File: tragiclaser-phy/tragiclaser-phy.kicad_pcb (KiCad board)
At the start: 4 copper layers, 105 x 28.5 mm, 79 parts, among them J1 XILINX_JTAG, J2 BEL_FUSE_0826-1G1T-23-F, K1 CONN_3_PWROUT, P1 CONN_01X12, U1 XC6SLX25-2FTG256C, U2 ADP322ACPZ-145-R7, U3 DNP, U4 100 MHz

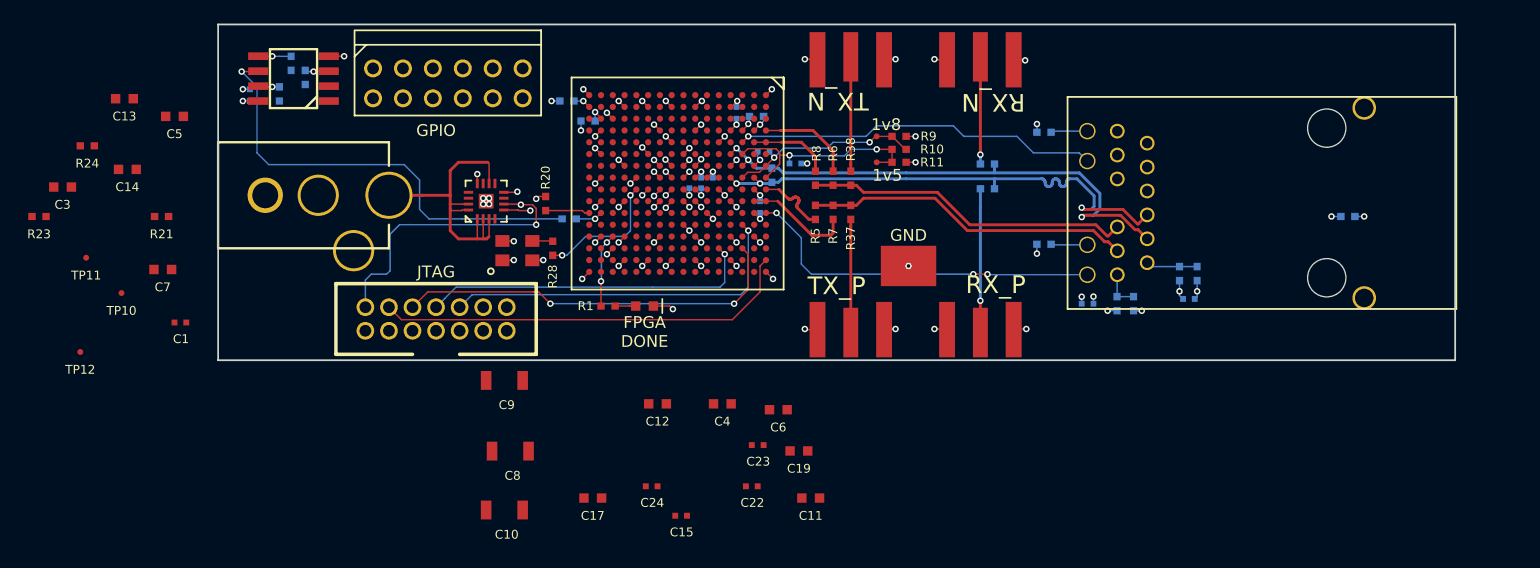
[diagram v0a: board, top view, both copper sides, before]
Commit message: Finished initial layout, ready for design review
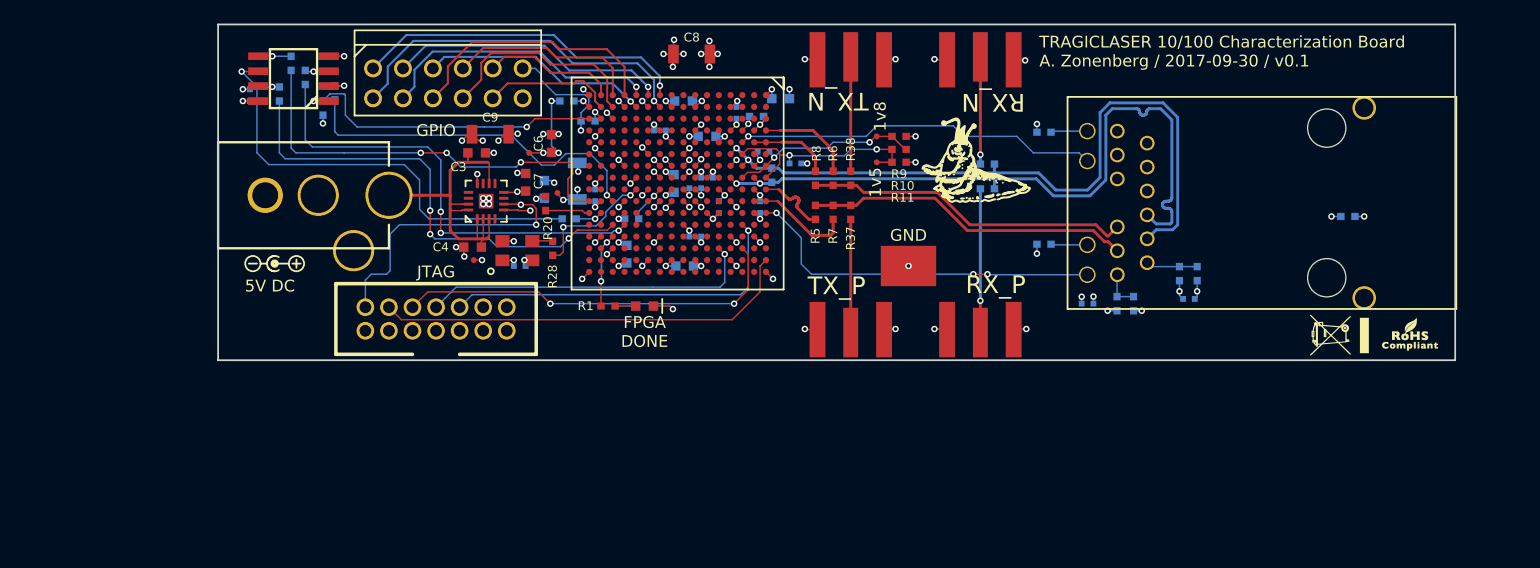
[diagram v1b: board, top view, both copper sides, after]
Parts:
- added G***: LOGO, azonenberg_pcb:LONGTHING-1200DPI, F.Cu at (142.9, 45.4)
- added G***: LOGO, w_logo:Logo_silk_WEEE_3.4x5mm, F.Cu at (173.2, 59.9)
- added G***: LOGO, w_logo:Logo_silk_ROHS_5x2.8mm, F.Cu at (179.2, 59.8)
- added G***: LOGO, w_logo:Logo_silk_polarity_center_5x1.4mm, F.Cu at (82.8, 53.8)
- C1, C10, C11, C12, C13, C14, C15, C17, C19, C22, C23, C24, C5, R21, R23, R24: moved to B.Cu
- moved C14 55.8 mm to (125.8, 39.8), turned to 180 degrees
- moved C13 47.2 mm to (116.7, 47.0), turned to 90 degrees
- moved TP12 42.7 mm to (106.8, 47.8)
- moved R21 39.9 mm to (113.1, 50.0), turned to 180 degrees
- moved TP11 38.6 mm to (104.4, 44.4)
- moved C8 37.1 mm to (118.2, 36.0)
- moved C11 35.4 mm to (117.5, 40.0)
- moved C3 35.3 mm to (100.0, 44.4)
- moved C5 32.0 mm to (105.7, 47.5), turned to 90 degrees
- moved C7 31.7 mm to (104.1, 46.9), turned to 90 degrees
- moved TP10 30.0 mm to (99.7, 53.5)
- moved C6 29.7 mm to (106.3, 43.6), turned to 90 degrees
- moved C1 29.2 mm to (103.6, 54.0)
- moved C10 28.6 mm to (108.5, 46.8), turned to 90 degrees
- moved C22 28.1 mm to (110.0, 48.0), turned to 270 degrees
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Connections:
- U1 pad A12: /PHY/GPIO1 -> Net-(U1-PadA12)
- U1 pad A13: /PHY/GPIO3 -> Net-(U1-PadA13)
- U1 pad A14: /PHY/GPIO5 -> Net-(U1-PadA14)
- U1 pad A2: (no net) -> Net-(U1-PadA2)
- U1 pad A3: (no net) -> Net-(U1-PadA3)
- U1 pad A6: /PHY/GPIO8 -> Net-(U1-PadA6)
- U1 pad B1: (no net) -> Net-(U1-PadB1)
- U1 pad B12: /PHY/GPIO0 -> Net-(U1-PadB12)
- U1 pad B14: /PHY/GPIO4 -> Net-(U1-PadB14)
- U1 pad B2: (no net) -> Net-(U1-PadB2)
- U1 pad B3: (no net) -> Net-(U1-PadB3)
- U1 pad B6: /PHY/GPIO7 -> Net-(U1-PadB6)
- U1 pad C1: (no net) -> Net-(U1-PadC1)
- U1 pad C11: /PHY/GPIO9 -> Net-(U1-PadC11)
- U1 pad C13: /PHY/GPIO2 -> Net-(U1-PadC13)
- U1 pad C2: (no net) -> Net-(U1-PadC2)
- U1 pad C3: (no net) -> Net-(U1-PadC3)
- U1 pad C9: /PHY/GPIO6 -> Net-(U1-PadC9)
- U1 pad D1: (no net) -> Net-(U1-PadD1)
- U1 pad D3: (no net) -> Net-(U1-PadD3)
- U1 pad E1: (no net) -> Net-(U1-PadE1)
- U1 pad E2: (no net) -> Net-(U1-PadE2)
- U1 pad E3: (no net) -> Net-(U1-PadE3)
- U1 pad E4: (no net) -> Net-(U1-PadE4)
- U1 pad F1: (no net) -> Net-(U1-PadF1)
- U1 pad F2: (no net) -> Net-(U1-PadF2)
- U1 pad F3: (no net) -> Net-(U1-PadF3)
- U1 pad F4: (no net) -> Net-(U1-PadF4)
- U1 pad F5: (no net) -> Net-(U1-PadF5)
- U1 pad F6: (no net) -> Net-(U1-PadF6)
- U1 pad G1: (no net) -> Net-(U1-PadG1)
- U1 pad G3: (no net) -> Net-(U1-PadG3)
- U1 pad G5: (no net) -> Net-(U1-PadG5)
- U1 pad G6: (no net) -> Net-(U1-PadG6)
- U1 pad H1: (no net) -> Net-(U1-PadH1)
- U1 pad H2: (no net) -> Net-(U1-PadH2)
- U1 pad H3: (no net) -> Net-(U1-PadH3)
- U1 pad H4: (no net) -> Net-(U1-PadH4)
- U1 pad H5: (no net) -> Net-(U1-PadH5)
- U1 pad J1: (no net) -> Net-(U1-PadJ1)
- U1 pad J3: (no net) -> Net-(U1-PadJ3)
- U1 pad J4: (no net) -> Net-(U1-PadJ4)
- U1 pad J6: (no net) -> Net-(U1-PadJ6)
- U1 pad K1: (no net) -> /PHY/GPIO0
- U1 pad K2: (no net) -> /PHY/GPIO1
- U1 pad K3: (no net) -> Net-(U1-PadK3)
- U1 pad K5: (no net) -> Net-(U1-PadK5)
- U1 pad K6: (no net) -> Net-(U1-PadK6)
- U1 pad L1: (no net) -> /PHY/GPIO2
- U1 pad L3: (no net) -> Net-(U1-PadL3)
- U1 pad L4: (no net) -> Net-(U1-PadL4)
- U1 pad L5: (no net) -> Net-(U1-PadL5)
- U1 pad M1: (no net) -> /PHY/GPIO3
- U1 pad M2: (no net) -> /PHY/GPIO4
- U1 pad M3: (no net) -> Net-(U1-PadM3)
- U1 pad M4: (no net) -> Net-(U1-PadM4)
- U1 pad M5: (no net) -> Net-(U1-PadM5)
- U1 pad N1: (no net) -> /PHY/GPIO5
- U1 pad N3: (no net) -> Net-(U1-PadN3)
- U1 pad N4: (no net) -> Net-(U1-PadN4)
- U1 pad P1: (no net) -> /PHY/GPIO6
- U1 pad P2: (no net) -> /PHY/GPIO7
- U1 pad R1: (no net) -> /PHY/GPIO8
- U1 pad R2: (no net) -> /PHY/GPIO9
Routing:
- net /3V3: track 188.8 -> 246.6 mm, vias 30 -> 37
- net /GND: track 340.8 -> 396.4 mm, vias 53 -> 68
- net /Boot/Config/FLASH_DQ3: track 0.00 -> 40.0 mm, vias 0 -> 3
- net /Boot/Config/FLASH_DQ2: track 0.00 -> 39.0 mm, vias 0 -> 3
- net /Boot/Config/FLASH_DQ0: track 0.00 -> 36.2 mm, vias 0 -> 3
- net /Boot/Config/FLASH_DQ1: track 0.00 -> 30.8 mm, vias 0 -> 1
- net /PHY/GPIO1: track 0.00 -> 30.6 mm, vias 0 -> 1
- net /PHY/GPIO0: track 0.00 -> 28.6 mm, vias 0 -> 1
- net /Boot/Config/FLASH_CS_N: track 0.00 -> 27.4 mm, vias 0 -> 2
- net /PHY/GPIO3: track 0.00 -> 24.2 mm, vias 0 -> 1
- net /PHY/GPIO2: track 0.00 -> 23.8 mm, vias 0 -> 1
- net /PHY/GPIO5: track 0.00 -> 22.4 mm
- net /PHY/GPIO4: track 0.00 -> 19.4 mm, vias 0 -> 1
- net /PHY/GPIO7: track 0.00 -> 18.2 mm
- net /PHY/GPIO6: track 0.00 -> 16.5 mm
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- added copper zone on In2.Cu, net /1V2
- added copper zone on In2.Cu, net /2V5
- added copper zone on In2.Cu, net /3V3
- added copper zone on In1.Cu, net /GND
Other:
- board text added: "5V DC"
- board text added: "TRAGICLASER 10/100 Characterization Board A. Zonenberg / 2017-09-30 / v0.1"

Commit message: Updated a few export settings during design review
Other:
- board text added: "TRAGICLASER 10/100 Characterization Board A. Zonenberg / 2017-10-05 / v0.1"
- board text removed: "TRAGICLASER 10/100 Characterization Board A. Zonenberg / 2017-09-30 / v0.1"
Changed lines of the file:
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@@
     (visible_elements FFFDFF7F)
     (pcbplotparams
-      (layerselection 0x00030_ffffffff)
-      (usegerberextensions false)
+      (layerselection 0x010f4_ffffffff)
+      (usegerberextensions true)
       (excludeedgelayer true)
       (linewidth 0.100000)
@@
       (outputformat 1)
       (mirror false)
-      (drillshape 1)
+      (drillshape 0)
       (scaleselection 1)
-      (outputdirectory ""))
+      (outputdirectory output/))
   )
   (net 0 "")
@@
     (add_net "Net-(U2-Pad9)")
   )
+  (module azonenberg_pcb:CONN_SMA_EDGE_SAMTEC_SMA_J_P_H_ST_EM1 (layer F.Cu)
+    (at 142.7 61.75)
+    (fp_text reference TP4 (at 0 3.1) (layer F.SilkS) hide
+      (effects (font (size 0.75 0.75) (thickness 0.15)))
+    )
+    (fp_text value SMA (at 0 1.6) (layer F.Fab)
+      (effects (font (size 0.75 0.75) (thickness 0.15)))
+    )
+    (pad 2 smd rect (at -2.825 -2.35) (size 1.35 4.7) (layers F.Cu F.Paste F.Mask)
+      (net 3 /GND))
+    (pad 2 smd rect (at 2.825 -2.35) (size 1.35 4.7) (layers F.Cu F.Paste F.Mask)
+      (net 3 /GND))
+    (pad 1 smd rect (at 0 -2.1) (size 1.27 4.2) (layers F.Cu F.Paste F.Mask)
+      (net 47 "Net-(R33-Pad1)"))
+    (model :SAMTEC:SMA-J-P-H-ST-EM1.stp
+      (at (xyz 0 -0.05905511811023623 0))
+      (scale (xyz 1 1 1))
+      (rotate (xyz 0 -90 180))
+    )
+  )
+  (module azonenberg_pcb:CONN_SMA_EDGE_SAMTEC_SMA_J_P_H_ST_EM1 (layer F.Cu)
+    (at 131.7 34.15 180)
+    (fp_text reference TP6 (at 0 3.1 180) (layer F.SilkS) hide
+      (effects (font (size 0.75 0.75) (thickness 0.15)))
+    )
+    (fp_text value SMA (at 0 1.6 180) (layer F.Fab)
+      (effects (font (size 0.75 0.75) (thickness 0.15)))
+    )
+    (pad 2 smd rect (at -2.825 -2.35 180) (size 1.35 4.7) (layers F.Cu F.Paste F.Mask)
+      (net 3 /GND))
+    (pad 2 smd rect (at 2.825 -2.35 180) (size 1.35 4.7) (layers F.Cu F.Paste F.Mask)
+      (net 3 /GND))
+    (pad 1 smd rect (at 0 -2.1 180) (size 1.27 4.2) (layers F.Cu F.Paste F.Mask)
+      (net 34 "Net-(R38-Pad2)"))
+    (model :SAMTEC:SMA-J-P-H-ST-EM1.stp
+      (at (xyz 0 -0.05905511811023623 0))
+      (scale (xyz 1 1 1))
+      (rotate (xyz 0 -90 180))
+    )
+  )
+  (module azonenberg_pcb:CONN_SMA_EDGE_SAMTEC_SMA_J_P_H_ST_EM1 (layer F.Cu)
+    (at 131.7 61.75)
+    (fp_text reference TP1 (at 0 3.1) (layer F.SilkS) hide
+      (effects (font (size 0.75 0.75) (thickness 0.15)))
+    )
+    (fp_text value SMA (at 0 1.6) (layer F.Fab)
+      (effects (font (size 0.75 0.75) (thickness 0.15)))
+    )
+    (pad 2 smd rect (at -2.825 -2.35) (size 1.35 4.7) (layers F.Cu F.Paste F.Mask)
+      (net 3 /GND))
+    (pad 2 smd rect (at 2.825 -2.35) (size 1.35 4.7) (layers F.Cu F.Paste F.Mask)
+      (net 3 /GND))
+    (pad 1 smd rect (at 0 -2.1) (size 1.27 4.2) (layers F.Cu F.Paste F.Mask)
+      (net 32 "Net-(R37-Pad1)"))
+    (model :SAMTEC:SMA-J-P-H-ST-EM1.stp
+      (at (xyz 0 -0.05905511811023623 0))
+      (scale (xyz 1 1 1))
+      (rotate (xyz 0 -90 180))
+    )
+  )
+  (module azonenberg_pcb:CONN_SMA_EDGE_SAMTEC_SMA_J_P_H_ST_EM1 (layer F.Cu)
+    (at 142.7 34.15 180)
+    (fp_text reference TP5 (at 0 3.1 180) (layer F.SilkS) hide
+      (effects (font (size 0.75 0.75) (thickness 0.15)))
+    )
+    (fp_text value SMA (at 0 1.6 180) (layer F.Fab)
+      (effects (font (size 0.75 0.75) (thickness 0.15)))
+    )
+    (pad 2 smd rect (at -2.825 -2.35 180) (size 1.35 4.7) (layers F.Cu F.Paste F.Mask)
+      (net 3 /GND))
+    (pad 2 smd rect (at 2.825 -2.35 180) (size 1.35 4.7) (layers F.Cu F.Paste F.Mask)
+      (net 3 /GND))
+    (pad 1 smd rect (at 0 -2.1 180) (size 1.27 4.2) (layers F.Cu F.Paste F.Mask)
+      (net 31 "Net-(R34-Pad2)"))
+    (model :SAMTEC:SMA-J-P-H-ST-EM1.stp
+      (at (xyz 0 -0.05905511811023623 0))
+      (scale (xyz 1 1 1))
+      (rotate (xyz 0 -90 180))
+    )
+  )
   (module azonenberg_pcb:LONGTHING-1200DPI locked (layer F.Cu)
     (at 142.9 45.4)
@@
     )
   )
-  (module azonenberg_pcb:CONN_SMA_EDGE_SAMTEC_SMA_J_P_H_ST_EM1 (layer F.Cu)
-    (at 142.7 61.75)
-    (fp_text reference TP4 (at 0 3.1) (layer F.SilkS) hide
-      (effects (font (size 0.75 0.75) (thickness 0.15)))
-    )
-    (fp_text value SMA (at 0 1.6) (layer F.Fab)
-      (effects (font (size 0.75 0.75) (thickness 0.15)))
-    )
-    (pad 1 smd rect (at 0 -2.1) (size 1.27 4.2) (layers F.Cu F.Paste F.Mask)
-      (net 47 "Net-(R33-Pad1)"))
-    (pad 2 smd rect (at 2.825 -2.35) (size 1.35 4.7) (layers F.Cu F.Paste F.Mask)
-      (net 3 /GND))
-    (pad 2 smd rect (at -2.825 -2.35) (size 1.35 4.7) (layers F.Cu F.Paste F.Mask)
-      (net 3 /GND))
-    (model /nfs4/home/azonenberg/kicad-libs/3rdparty/walter/conn_rf/sma_90_r300.124.403.wrl
-      (at (xyz 0 -0.03937007874015748 0))
-      (scale (xyz 1 1 1))
-      (rotate (xyz 0 0 0))
-    )
-  )
-  (module azonenberg_pcb:CONN_SMA_EDGE_SAMTEC_SMA_J_P_H_ST_EM1 (layer F.Cu)
-    (at 131.7 34.15 180)
-    (fp_text reference TP6 (at 0 3.1 180) (layer F.SilkS) hide
-      (effects (font (size 0.75 0.75) (thickness 0.15)))
-    )
-    (fp_text value SMA (at 0 1.6 180) (layer F.Fab)
-      (effects (font (size 0.75 0.75) (thickness 0.15)))
-    )
-    (pad 2 smd rect (at -2.825 -2.35 180) (size 1.35 4.7) (layers F.Cu F.Paste F.Mask)
-      (net 3 /GND))
-    (pad 2 smd rect (at 2.825 -2.35 180) (size 1.35 4.7) (layers F.Cu F.Paste F.Mask)
-      (net 3 /GND))
-    (pad 1 smd rect (at 0 -2.1 180) (size 1.27 4.2) (layers F.Cu F.Paste F.Mask)
-      (net 34 "Net-(R38-Pad2)"))
-    (model /nfs4/home/azonenberg/kicad-libs/3rdparty/walter/conn_rf/sma_90_r300.124.403.wrl
-      (at (xyz 0 -0.03937007874015748 0))
-      (scale (xyz 1 1 1))
-      (rotate (xyz 0 0 0))
-    )
-  )
-  (module azonenberg_pcb:CONN_SMA_EDGE_SAMTEC_SMA_J_P_H_ST_EM1 (layer F.Cu)
-    (at 131.7 61.75)
-    (fp_text reference TP1 (at 0 3.1) (layer F.SilkS) hide
-      (effects (font (size 0.75 0.75) (thickness 0.15)))
-    )
-    (fp_text value SMA (at 0 1.6) (layer F.Fab)
-      (effects (font (size 0.75 0.75) (thickness 0.15)))
-    )
-    (pad 2 smd rect (at -2.825 -2.35) (size 1.35 4.7) (layers F.Cu F.Paste F.Mask)
-      (net 3 /GND))
-    (pad 2 smd rect (at 2.825 -2.35) (size 1.35 4.7) (layers F.Cu F.Paste F.Mask)
-      (net 3 /GND))
-    (pad 1 smd rect (at 0 -2.1) (size 1.27 4.2) (layers F.Cu F.Paste F.Mask)
-      (net 32 "Net-(R37-Pad1)"))
-    (model /nfs4/home/azonenberg/kicad-libs/3rdparty/walter/conn_rf/sma_90_r300.124.403.wrl
-      (at (xyz 0 -0.03937007874015748 0))
-      (scale (xyz 1 1 1))
-      (rotate (xyz 0 0 0))
-    )
-  )
-  (module azonenberg_pcb:CONN_SMA_EDGE_SAMTEC_SMA_J_P_H_ST_EM1 (layer F.Cu)
-    (at 142.7 34.15 180)
-    (fp_text reference TP5 (at 0 3.1 180) (layer F.SilkS) hide
-      (effects (font (size 0.75 0.75) (thickness 0.15)))
-    )
-    (fp_text value SMA (at 0 1.6 180) (layer F.Fab)
-      (effects (font (size 0.75 0.75) (thickness 0.15)))
-    )
-    (pad 1 smd rect (at 0 -2.1 180) (size 1.27 4.2) (layers F.Cu F.Paste F.Mask)
-      (net 31 "Net-(R34-Pad2)"))
-    (pad 2 smd rect (at 2.825 -2.35 180) (size 1.35 4.7) (layers F.Cu F.Paste F.Mask)
-      (net 3 /GND))
-    (pad 2 smd rect (at -2.825 -2.35 180) (size 1.35 4.7) (layers F.Cu F.Paste F.Mask)
-      (net 3 /GND))
-    (model /nfs4/home/azonenberg/kicad-libs/3rdparty/walter/conn_rf/sma_90_r300.124.403.wrl
-      (at (xyz 0 -0.03937007874015748 0))
-      (scale (xyz 1 1 1))
-      (rotate (xyz 0 0 0))
-    )
-  )
   (module azonenberg_pcb:EIA_0402_CAP_NOSILK (layer B.Cu)
     (at 110 47.999999 270)
@@
     (effects (font (size 1 1) (thickness 0.15)))
   )
-  (gr_text "TRAGICLASER 10/100 Characterization Board\nA. Zonenberg / 2017-09-30 / v0.1" (at 147.7 35.8) (layer F.SilkS)
+  (gr_text "TRAGICLASER 10/100 Characterization Board\nA. Zonenberg / 2017-10-05 / v0.1" (at 147.7 35.8) (layer F.SilkS)
     (effects (font (size 1 1) (thickness 0.15)) (justify left))
   )

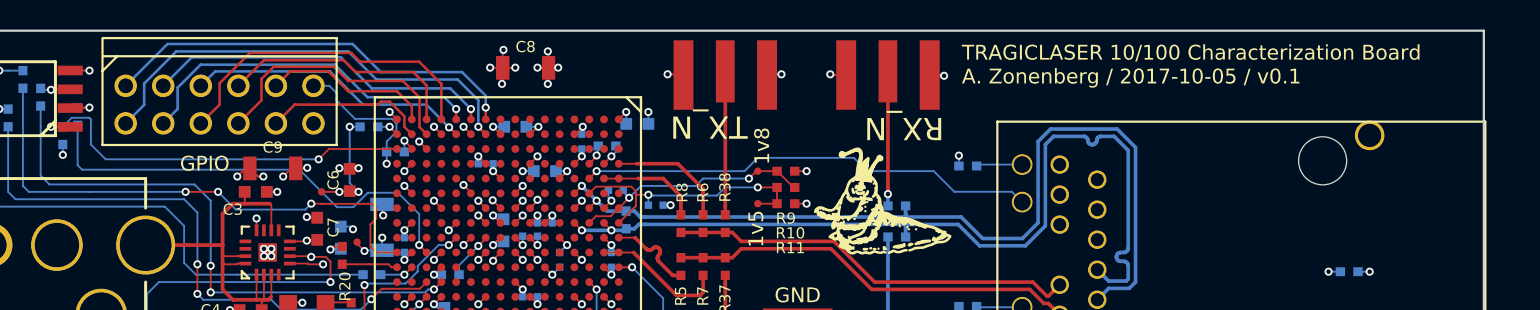
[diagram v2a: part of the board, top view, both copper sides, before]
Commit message: Updated export settings, moved a bit of silkscreen text
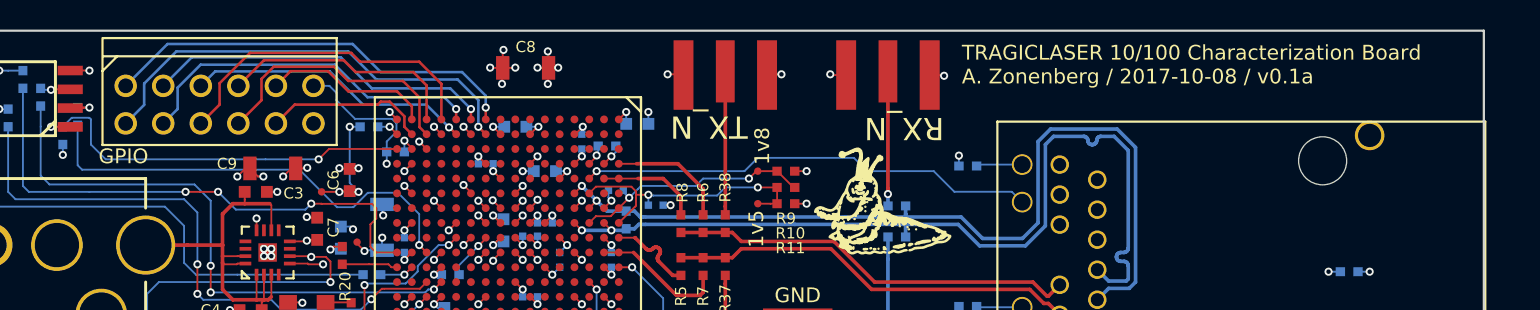
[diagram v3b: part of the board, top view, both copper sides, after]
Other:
- board text added: "TRAGICLASER 10/100 Characterization Board A. Zonenberg / 2017-10-08 / v0.1a"
- board text removed: "TRAGICLASER 10/100 Characterization Board A. Zonenberg / 2017-10-05 / v0.1"
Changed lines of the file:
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@@
     (visible_elements FFFDFF7F)
     (pcbplotparams
-      (layerselection 0x010f4_ffffffff)
+      (layerselection 0x010fc_ffffffff)
       (usegerberextensions true)
       (excludeedgelayer true)
@@
   (module azonenberg_pcb:EIA_0402_RES_NOSILK (layer B.Cu)
     (at 87.9 39.3 270)
-    (fp_text reference R24 (at -0.9 -0.1 270) (layer B.SilkS)
+    (fp_text reference R24 (at -2.3 -0.1 270) (layer B.SilkS)
       (effects (font (size 0.75 0.75) (thickness 0.15)) (justify mirror))
     )
@@
   (module azonenberg_pcb:EIA_0603_CAP_NOSILK (layer F.Cu)
     (at 99.95 44.4)
-    (fp_text reference C3 (at -1.55 1.2) (layer F.SilkS)
+    (fp_text reference C3 (at 2.55 0.1) (layer F.SilkS)
       (effects (font (size 0.75 0.75) (thickness 0.15)))
     )
@@
   (module azonenberg_pcb:EIA_1206_CAP_NOSILK (layer F.Cu)
     (at 101.1 42.8)
-    (fp_text reference C9 (at 0 -1.4) (layer F.SilkS)
+    (fp_text reference C9 (at -3.1 -0.3) (layer F.SilkS)
       (effects (font (size 0.75 0.75) (thickness 0.15)))
     )
@@
     (effects (font (size 1 1) (thickness 0.15)))
   )
-  (gr_text "TRAGICLASER 10/100 Characterization Board\nA. Zonenberg / 2017-10-05 / v0.1" (at 147.7 35.8) (layer F.SilkS)
+  (gr_text "TRAGICLASER 10/100 Characterization Board\nA. Zonenberg / 2017-10-08 / v0.1a" (at 147.7 35.8) (layer F.SilkS)
     (effects (font (size 1 1) (thickness 0.15)) (justify left))
   )
@@
     (effects (font (size 1 1) (thickness 0.15)))
   )
-  (gr_text GPIO (at 96.5 42.5) (layer F.SilkS)
+  (gr_text GPIO (at 91 42) (layer F.SilkS)
     (effects (font (size 1 1) (thickness 0.15)))
   )
